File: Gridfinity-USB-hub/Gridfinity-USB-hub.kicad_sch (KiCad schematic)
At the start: 18 parts, among them J1 USB_C_Receptacle_USB2.0_16P, J2 QWIIC, U1 CH334F, Y1 12MHz

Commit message: USB Hub Board as order submitted on 9/6
This might get rejected by JLC for via sizes.
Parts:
- J2: FT Position Offset (none) -> 0,-0.381; FT Rotation Offset (none) -> 180
- U1: FT Rotation Offset (none) -> 180
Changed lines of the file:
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@@
+			)
+		)
+		(property "FT Position Offset" "0,-0.381"
+			(at 60.96 172.72 0)
+			(effects
+				(font
+					(size 1.27 1.27)
+				)
+				(hide yes)
+			)
+		)
+		(property "FT Rotation Offset" "180"
+			(at 60.96 172.72 0)
+			(effects
+				(font
+					(size 1.27 1.27)
+				)
+				(hide yes)
 			)
 		)
@@
 			(at 104.14 101.6 0)
 			(effects
+				(font
+					(size 1.27 1.27)
+				)
+				(hide yes)
+			)
+		)
+		(property "FT Position Offset" ""
+			(at 104.14 101.6 0)
+			(effects
+				(font
+					(size 1.27 1.27)
+				)
+				(hide yes)
+			)
+		)
+		(property "FT Rotation Offset" "180"
+			(at 104.14 101.6 0)
+			(effects

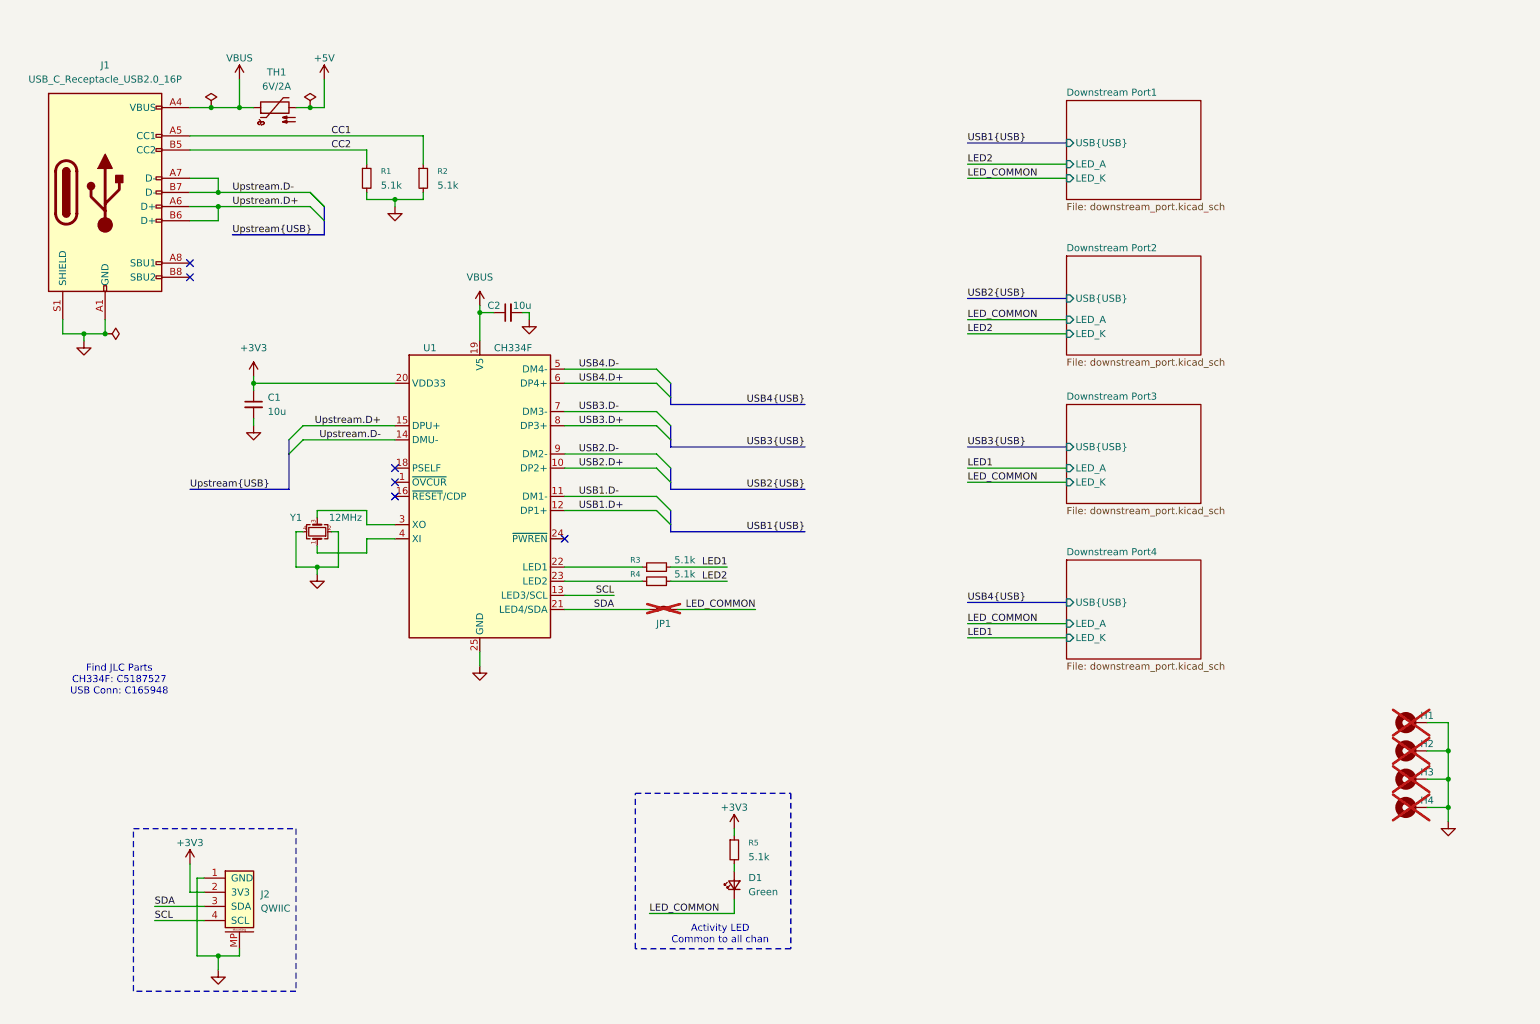
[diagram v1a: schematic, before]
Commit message: Update to USB Hub to use symbol in library.  Probably some other changes as well
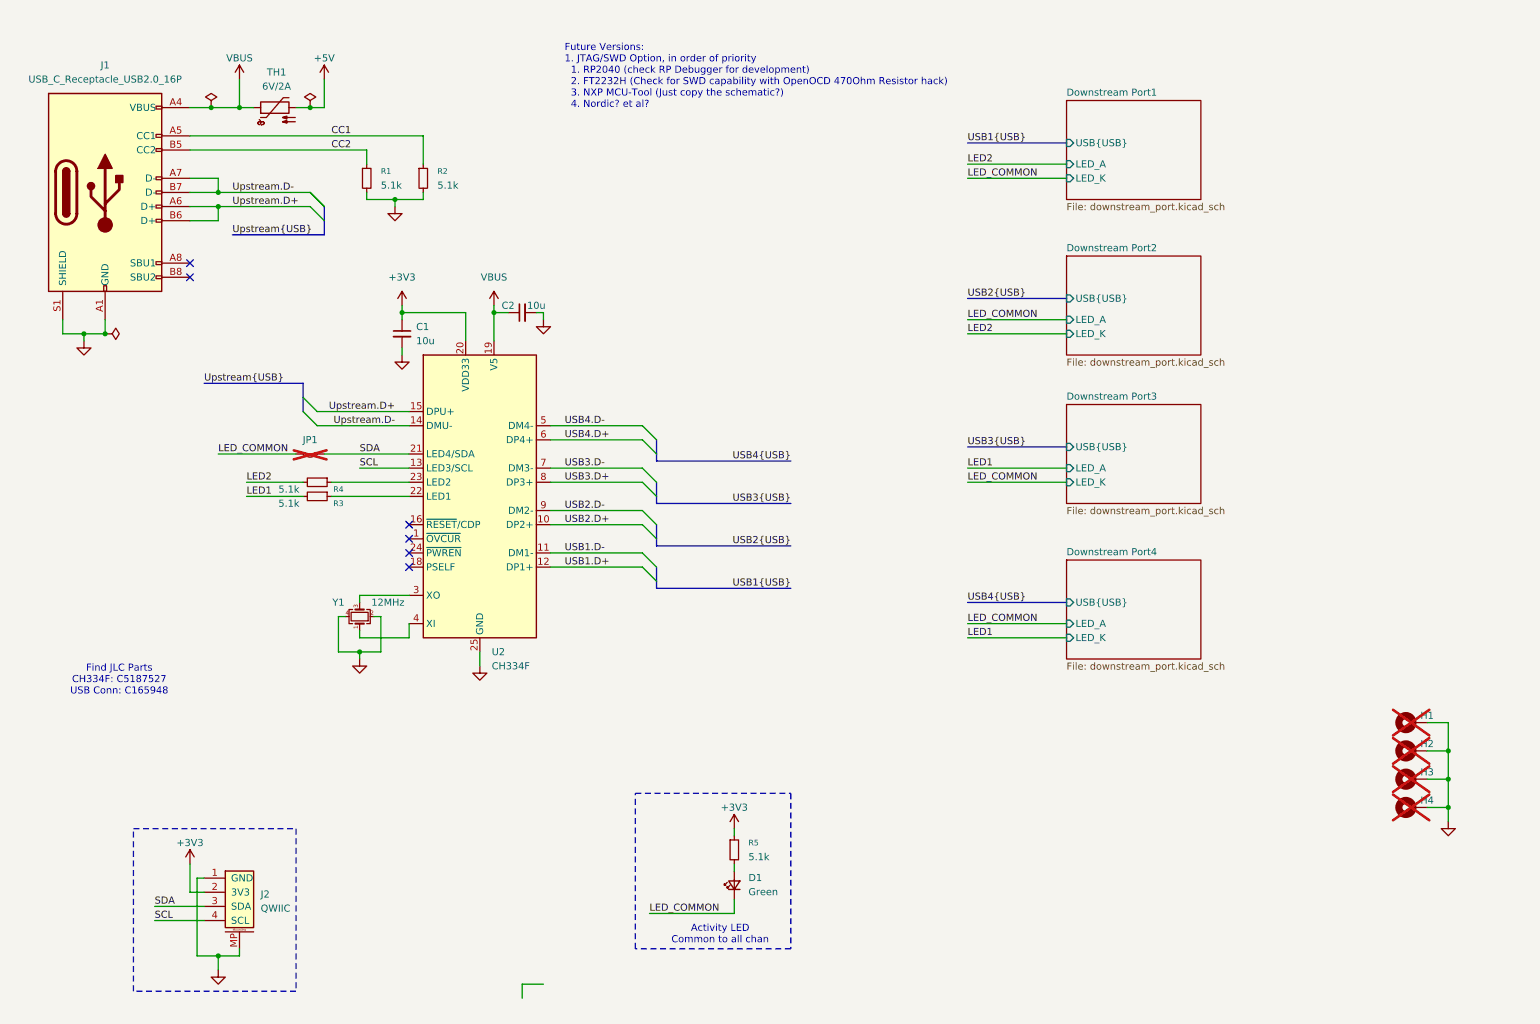
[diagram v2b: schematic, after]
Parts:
- removed U1: CH334F, Package_DFN_QFN:QFN-24-1EP_4x4mm_P0.5mm_EP2.7x2.7mm, symbol Interface_USB:CH334F
- added U2: CH334F, Package_DFN_QFN:QFN-24-1EP_4x4mm_P0.5mm_EP2.7x2.7mm, symbol Interface_USB:CH334F
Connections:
- net +3V3: now also U2.20 (VDD33)
- net GND: now also U2.25 (GND)
- net SCL: now also U2.13 (LED3/SCL)
- net SDA: now also U2.21 (LED4/SDA)
- net USB1.D+: now also U2.12 (DP1+)
- net USB1.D-: now also U2.11 (DM1-)
- net USB2.D+: now also U2.10 (DP2+)
- net USB2.D-: now also U2.9 (DM2-)
- net USB3.D+: now also U2.8 (DP3+)
- net USB3.D-: now also U2.7 (DM3-)
- net USB4.D+: now also U2.6 (DP4+)
- net USB4.D-: now also U2.5 (DM4-)
- net Upstream.D+: now also U2.15 (DPU+)
- net Upstream.D-: now also U2.14 (DMU-)
- net VBUS: now also U2.19 (V5)
- net at R3.1: now also U2.22 (LED1)
- net at R4.1: now also U2.23 (LED2)
- net at Y1.3: now also U2.3 (XO)
- net at Y1.1: now also U2.4 (XI)
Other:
- note added: "Future Versions: 1. JTAG/SWD Option, in order of priority 1. RP2040 (check RP Debugger for development) 2. FT2232H (Check for SWD capability with OpenOCD 470Ohm Resistor hack) 3. NXP MCU-Tool (Just copy the schematic?) 4. Nordic? et al?"
- moved on the sheet: C1, C2, JP1, R3, R4, Y1

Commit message: Checkpoint, changing computers
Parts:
- removed C1, C2: 10u, Capacitor_SMD:C_0603_1608Metric, symbol Device:C_Small
- removed D1: Green, LED_SMD:LED_0603_1608Metric, symbol Device:LED_Small
- removed J1: USB_C_Receptacle_USB2.0_16P, Connector_USB:USB_C_Receptacle_G-Switch_GT-USB-7051x, symbol Connector:USB_C_Receptacle_USB2.0_16P
- removed J2: QWIIC, Connector_JST:JST_SH_BM04B-SRSS-TB_1x04-1MP_P1.00mm_Vertical, symbol SKEC_Symbols:Conn_QWIIC_Vertical
- removed JP1: Jumper_2_Small_Bridged, Jumper:SolderJumper-2_P1.3mm_Bridged_RoundedPad1.0x1.5mm, symbol Jumper:Jumper_2_Small_Bridged
- removed R1, R2, R3, R4, R5: 5.1k, Resistor_SMD:R_0402_1005Metric, symbol Device:R_Small
- removed TH1: 6V/2A, Resistor_SMD:R_0603_1608Metric, symbol Device:Thermistor_PTC
- removed U2: CH334F, Package_DFN_QFN:QFN-24-1EP_4x4mm_P0.5mm_EP2.7x2.7mm, symbol Interface_USB:CH334F
- removed Y1: 12MHz, Crystal:Crystal_SMD_2520-4Pin_2.5x2.0mm, symbol Device:Crystal_GND24_Small
- added D7: Green, LED_SMD:LED_0402_1005Metric, symbol Device:LED_Small
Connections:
- new net LED_MID.A: D7.2 (A)
- new net LED_MID.K: D7.1 (K)
- no-connect marks 6 -> 0
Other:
- added sheet JTAG_SWD (JTAG_SWD.kicad_sch)
- added sheet Power (power.kicad_sch)
- added sheet Serial_comms (Serial_comms.kicad_sch)
- added sheet USB_Hub (USB_Hub.kicad_sch)
- added sheet USB_Hub1 (USB_Hub.kicad_sch)
- added sheet Upstream (upstream.kicad_sch)
- sheet Downstream Port1 ports: added LED{LED}; removed LED_A, LED_K
- sheet Downstream Port2 ports: added LED{LED}; removed LED_A, LED_K
- sheet Downstream Port3 ports: added LED{LED}; removed LED_A, LED_K
- sheet Downstream Port4 ports: added LED{LED}; removed LED_A, LED_K
- note removed: "Activity LED Common to all chan"

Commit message: V2 complete, ready for review and polish
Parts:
- added J2: QWIIC, Connector_JST:JST_SH_BM04B-SRSS-TB_1x04-1MP_P1.00mm_Vertical, symbol SKEC_Symbols:Conn_QWIIC_Vertical
- added R34, R35: 10k, Resistor_SMD:R_0402_1005Metric, symbol Device:R_Small
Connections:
- net GND: now also J2.1 (GND), J2.MP
- new net +3V3: J2.2 (3V3), R34.1, R35.1
- new net SENSOR_I2C.SCL: J2.4 (SCL), R35.2
- new net SENSOR_I2C.SDA: J2.3 (SDA), R34.2
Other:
- sheet USB_Hub renamed USB_Hub0
- removed sheet JTAG_SWD
- added sheet Downstream Port5 (downstream_port_with_sensor.kicad_sch)
- added sheet Downstream Port6 (downstream_port_with_sensor.kicad_sch)
- note added: "I2C Addr: 0b1000010{r/w}"
- note added: "I2C Addr: 0b1000011{r/w}"

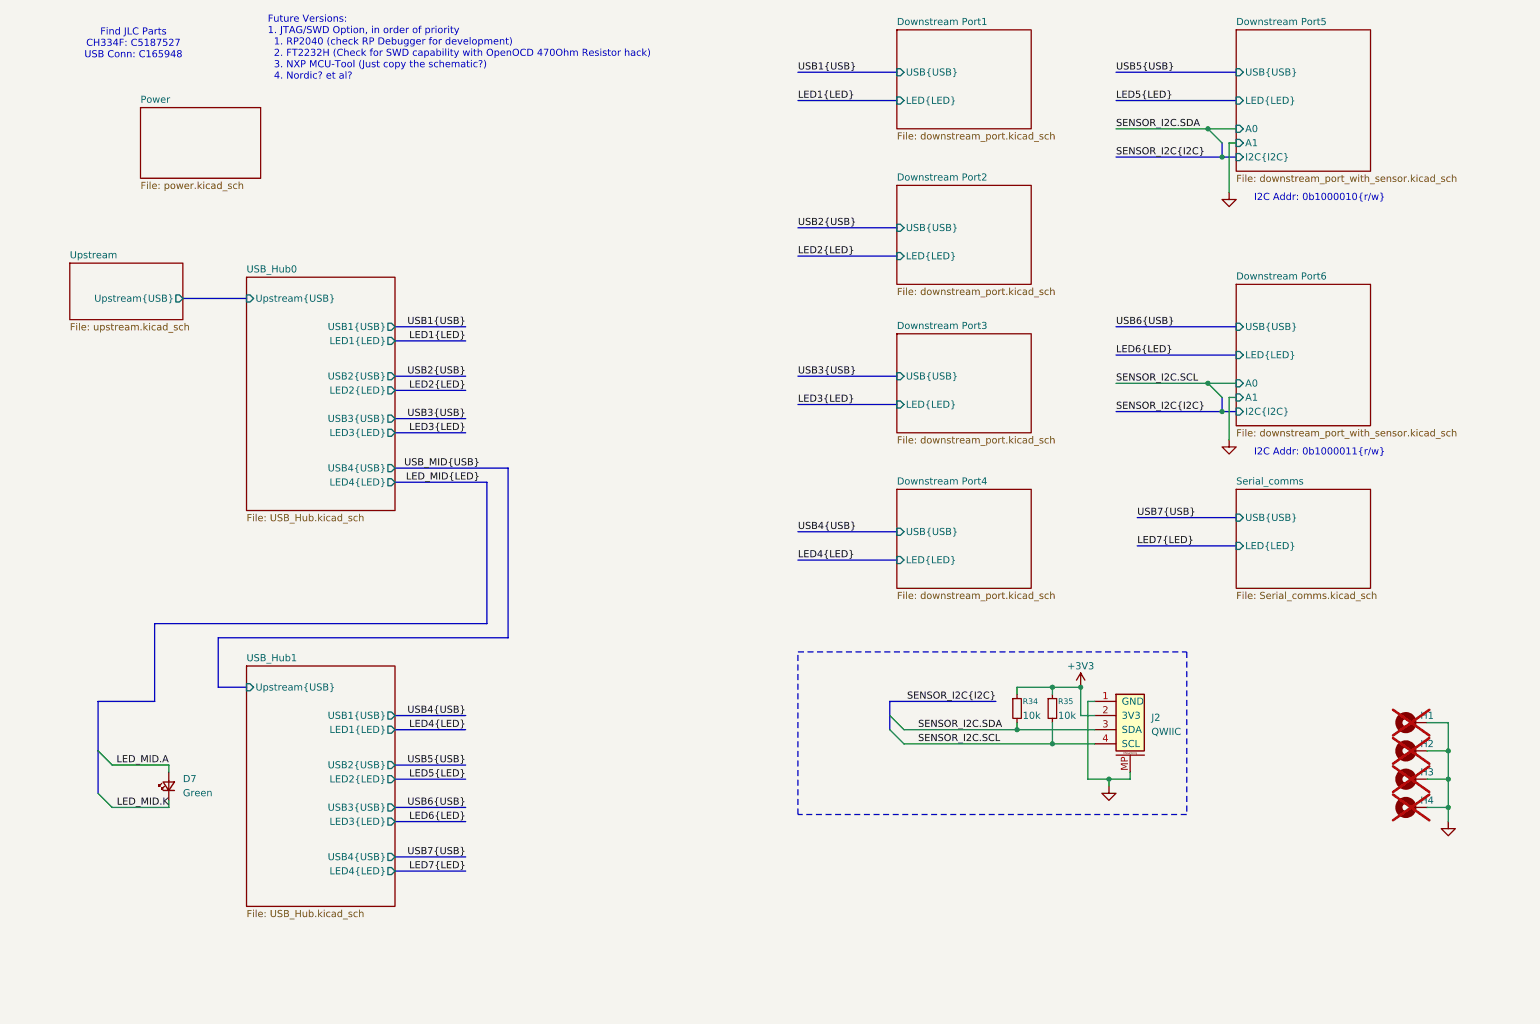
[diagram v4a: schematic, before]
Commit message: Add 3x channels of spare LEDs for general breadboard use, add silkscreen.  Ordered this version
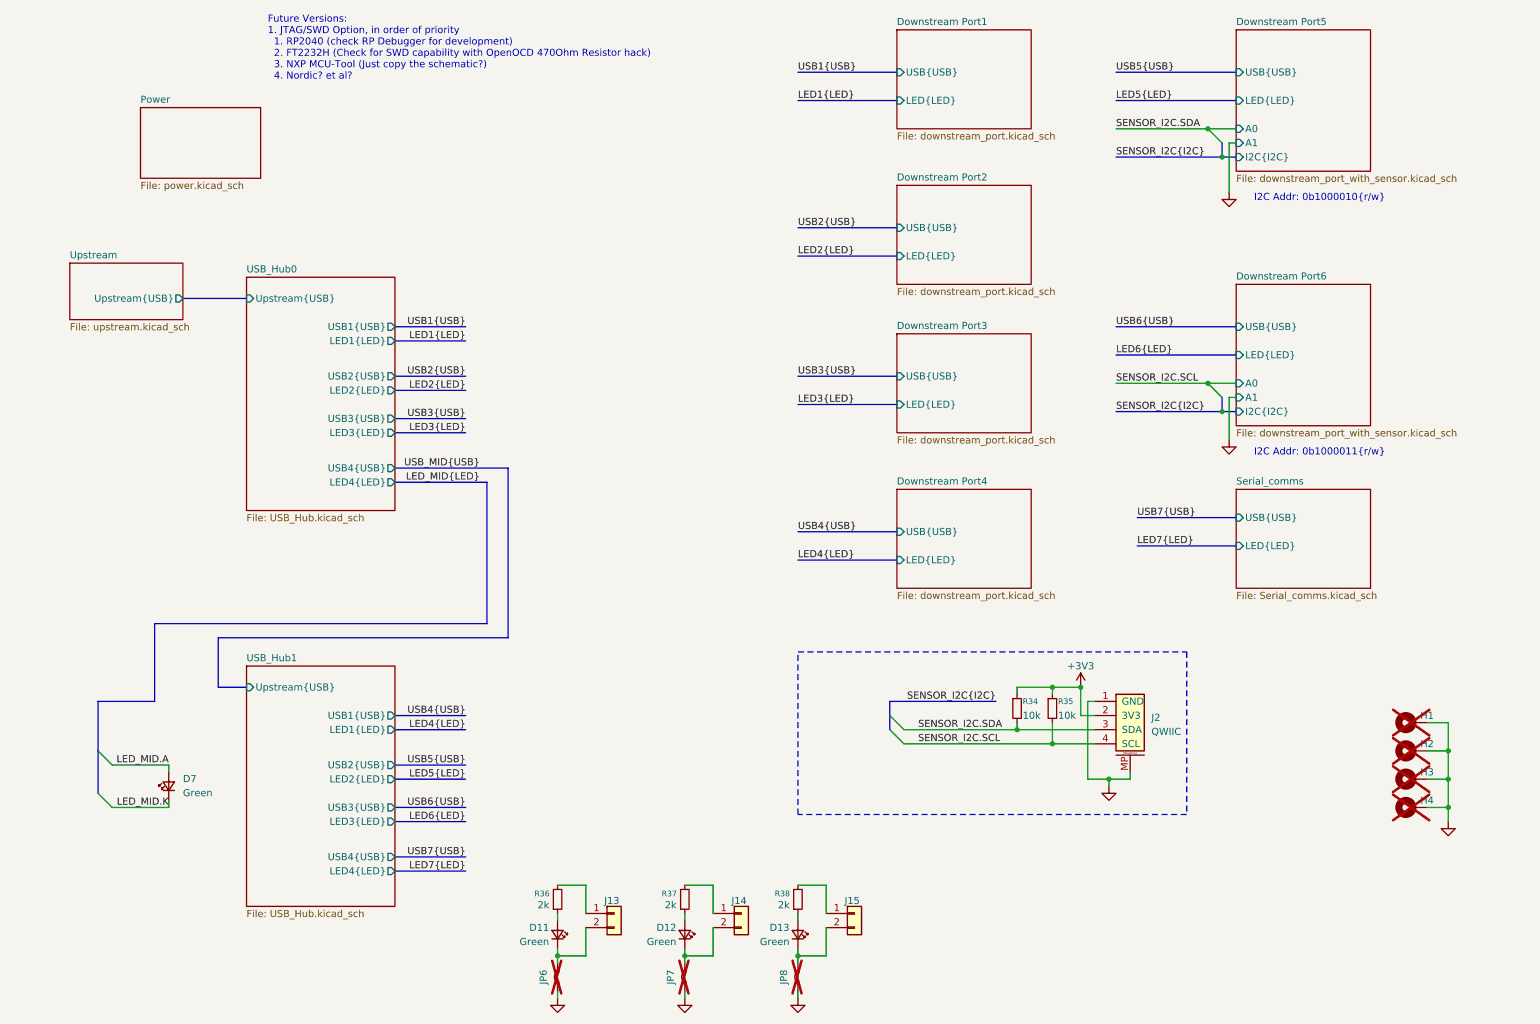
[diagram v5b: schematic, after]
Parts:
- added D11, D12, D13: Green, LED_SMD:LED_0402_1005Metric, symbol Device:LED_Small
- added J13, J14, J15: Conn_01x02, Connector_PinSocket_2.54mm:PinSocket_1x02_P2.54mm_Vertical, symbol Connector_Generic:Conn_01x02
- added JP6, JP7, JP8: Jumper_2_Small_Bridged, Jumper:SolderJumper-2_P1.3mm_Bridged2Bar_RoundedPad1.0x1.5mm, symbol Jumper:Jumper_2_Small_Bridged
- added R36, R37, R38: 2k, Resistor_SMD:R_0402_1005Metric, symbol Device:R_Small
- R34, R35: JLCPCB Part No. (none) -> C60490; MPN (none) -> RC0402FR-0710KL
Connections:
- net GND: now also JP6.2 (B), JP7.2 (B), JP8.2 (B)
- new net: D13.2 (A), R38.1
- new net: J15.1 (Pin_1), R38.2
- new net: D11.2 (A), R36.1
- new net: J13.1 (Pin_1), R36.2
- new net: D11.1 (K), J13.2 (Pin_2), JP6.1 (A)
- new net: D13.1 (K), J15.2 (Pin_2), JP8.1 (A)
- new net: D12.1 (K), J14.2 (Pin_2), JP7.1 (A)
- new net: D12.2 (A), R37.1
- new net: J14.1 (Pin_1), R37.2
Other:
- note removed: "Find JLC Parts CH334F: C5187527 USB Conn: C165948"
- company: (none) -> SK Electronics Consulting LLC
- title: (none) -> USB 2.0 Hub for Gridifinity
